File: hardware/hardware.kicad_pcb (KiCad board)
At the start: 2 copper layers, 83 x 54.5 mm, 15 parts, among them J1 Screw_Terminal_01x02, J2 Screw_Terminal_01x02, J3 Screw_Terminal_01x02, K1 RM85-2011-35-1005, K2 RM85-2011-35-1005, Q1 BC337, Q2 BC337, U1 XIAO-ESP32-C6

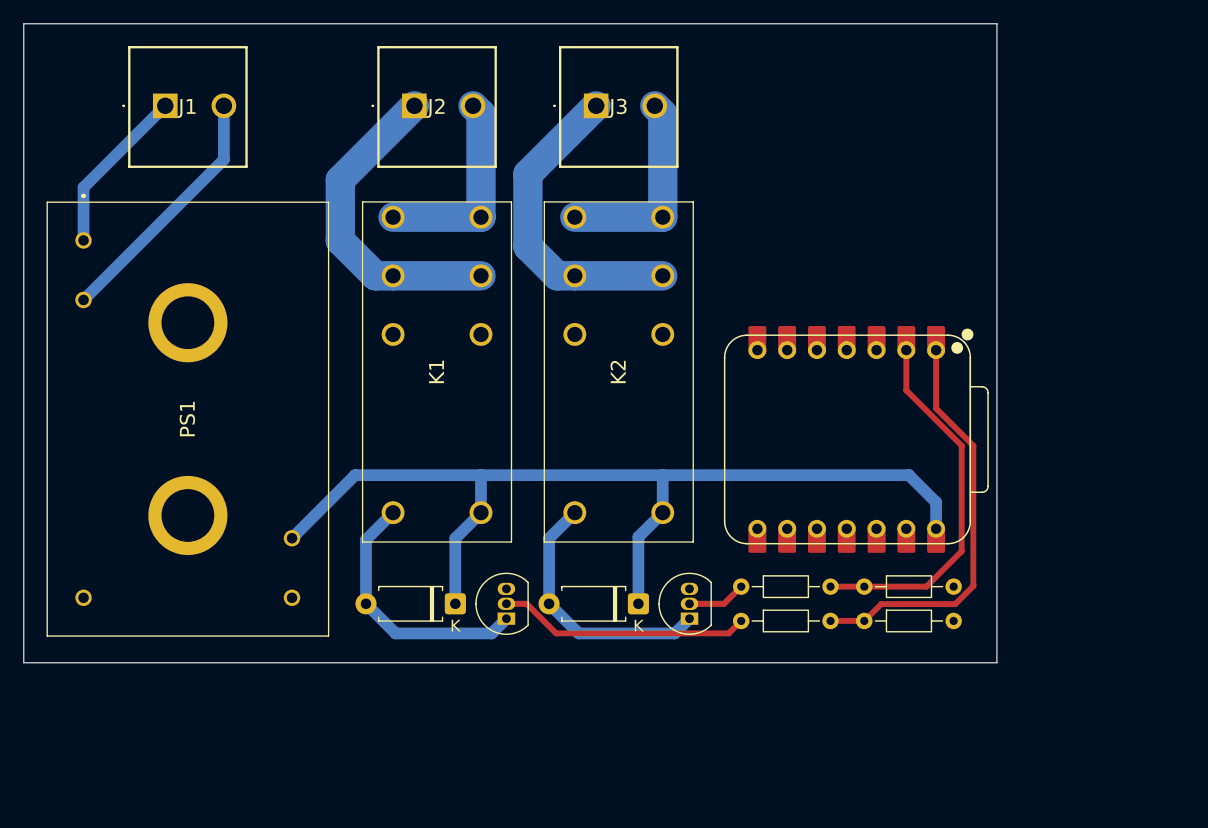
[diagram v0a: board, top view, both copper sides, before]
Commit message: Added GND fill zone
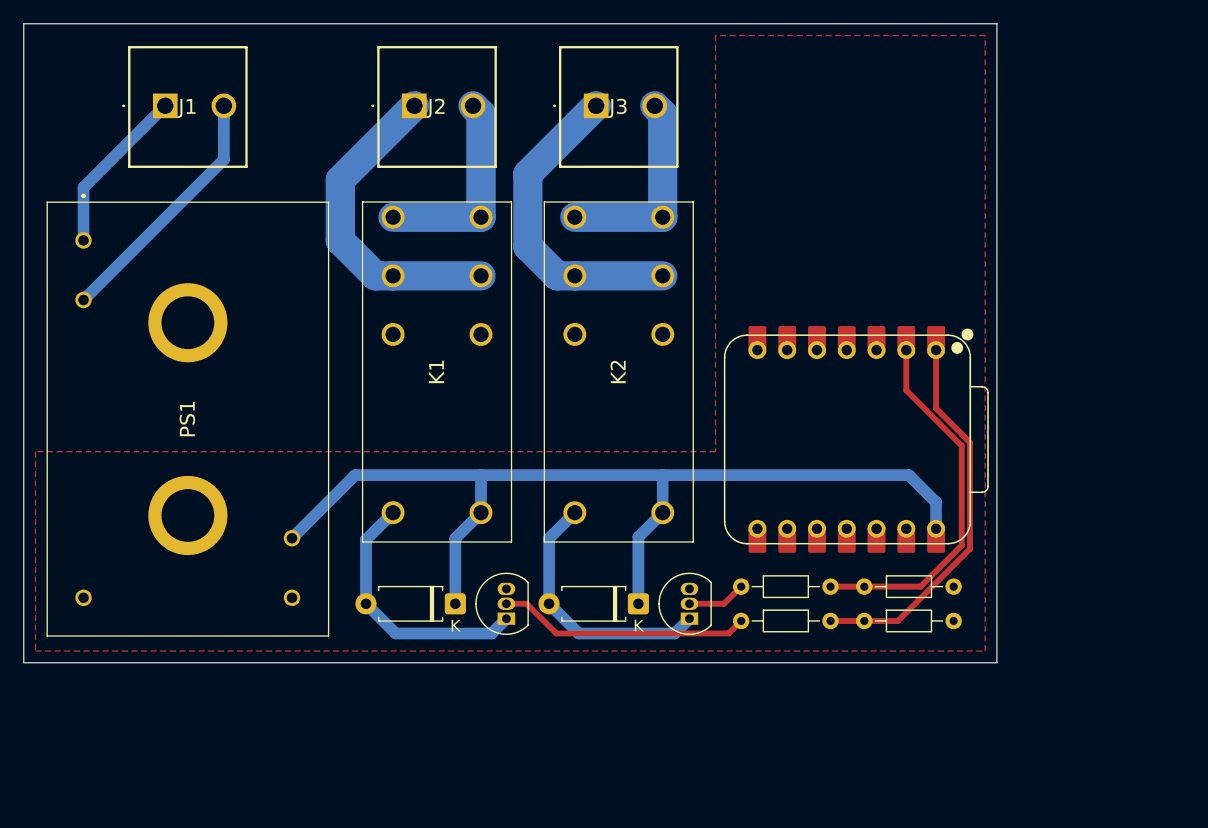
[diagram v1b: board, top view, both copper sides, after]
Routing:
- net RELAY_A_CTRL: track 34.9 -> 32.6 mm
- added copper zone on F.Cu, net GND
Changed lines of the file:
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@@
 	)
 	(segment
-		(start 88.12625 64.5)
-		(end 86.69 65.93625)
+		(start 92.8125 47.8125)
+		(end 92.8125 42.835)
 		(width 0.5)
 		(layer "F.Cu")
@@
 	)
 	(segment
-		(start 96 62.94651)
-		(end 94.44651 64.5)
+		(start 95 50.008636)
+		(end 95 50)
 		(width 0.5)
 		(layer "F.Cu")
@@
 	)
 	(segment
-		(start 94.44651 64.5)
-		(end 88.12625 64.5)
+		(start 89.555114 65.93625)
+		(end 95.701 59.790364)
 		(width 0.5)
 		(layer "F.Cu")
@@
 	)
 	(segment
-		(start 92.8125 42.835)
-		(end 92.8125 47.8125)
+		(start 95.701 50.709636)
+		(end 95 50.008636)
 		(width 0.5)
 		(layer "F.Cu")
@@
 	)
 	(segment
-		(start 92.8125 47.8125)
-		(end 96 51)
+		(start 86.69 65.93625)
+		(end 89.555114 65.93625)
 		(width 0.5)
 		(layer "F.Cu")
@@
 	)
 	(segment
-		(start 96 51)
-		(end 96 62.94651)
+		(start 95.701 59.790364)
+		(end 95.701 50.709636)
+		(width 0.5)
+		(layer "F.Cu")
+		(net 19)
+	)
+	(segment
+		(start 95 50)
+		(end 92.8125 47.8125)
 		(width 0.5)
 		(layer "F.Cu")
@@
 	)
 	(segment
-		(start 95 51)
-		(end 95 60)
-		(width 0.5)
-		(layer "F.Cu")
-		(net 20)
-	)
-	(segment
-		(start 91.99125 63.00875)
+		(start 83.81 63.00875)
 		(end 86.69 63.00875)
 		(width 0.5)
@@
 	)
 	(segment
-		(start 83.81 63.00875)
-		(end 86.69 63.00875)
+		(start 91.49125 63.00875)
+		(end 95 59.5)
+		(width 0.5)
+		(layer "F.Cu")
+		(net 20)
+	)
+	(segment
+		(start 86.69 63.00875)
+		(end 91.49125 63.00875)
 		(width 0.5)
 		(layer "F.Cu")
@@
 	)
 	(segment
-		(start 95 60)
-		(end 91.99125 63.00875)
+		(start 95 59.5)
+		(end 95 51)
 		(width 0.5)
 		(layer "F.Cu")
 		(net 20)
 	)
+	(zone
+		(net 16)
+		(net_name "GND")
+		(layer "F.Cu")
+		(hatch edge 0.5)
+		(connect_pads
+			(clearance 0.5)
+		)
+		(min_thickness 0.25)
+		(filled_areas_thickness no)
+		(fill yes
+			(thermal_gap 0.5)
+			(thermal_bridge_width 0.5)
+		)
+		(polygon
+			(pts
+				(xy 97 16) (xy 74 16) (xy 74 51.5) (xy 16 51.5) (xy 16 68.5) (xy 97 68.5)
+			)
+		)
+	)
 	(group ""

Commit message: Added mounting holes
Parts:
- added H1: MountingHole_Pad, MountingHole:MountingHole_2.2mm_M2_Pad, F.Cu at (110.0, 31.0)
- added H2: MountingHole, MountingHole:MountingHole_2.2mm_M2, F.Cu at (35.0, 31.0)
- moved D1 20.0 mm to (67.8, 76.5)
- moved D2 20.0 mm to (83.4, 76.5)
- moved K1 20.0 mm to (70.0, 48.5)
- moved K2 20.0 mm to (85.5, 48.5)
- moved R2 20.0 mm to (102.7, 78.0)
- moved R4 20.0 mm to (92.2, 78.0)
- moved U1 20.0 mm to (101.2, 62.5)
- moved J1 20.0 mm to (43.1, 34.0)
- moved J2 20.0 mm to (64.3, 34.0)
- moved J3 20.0 mm to (79.8, 34.0)
- moved PS1 20.0 mm to (36.1, 45.5)
- moved R5 20.0 mm to (92.2, 75.1)
- moved R6 20.0 mm to (102.7, 75.1)
- moved Q2 20.0 mm to (87.8, 77.8)
- moved Q1 20.0 mm to (72.2, 77.8)

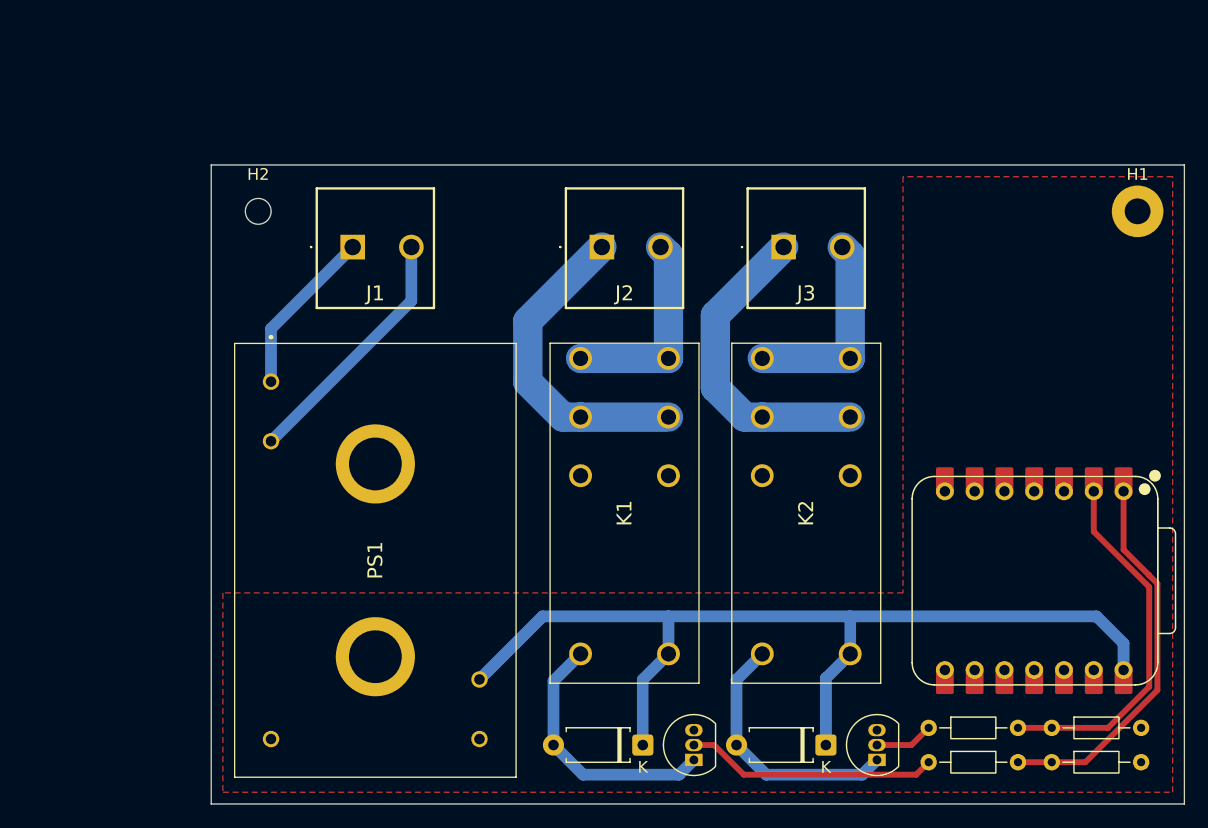
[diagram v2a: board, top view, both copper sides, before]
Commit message: Updated screw terminals
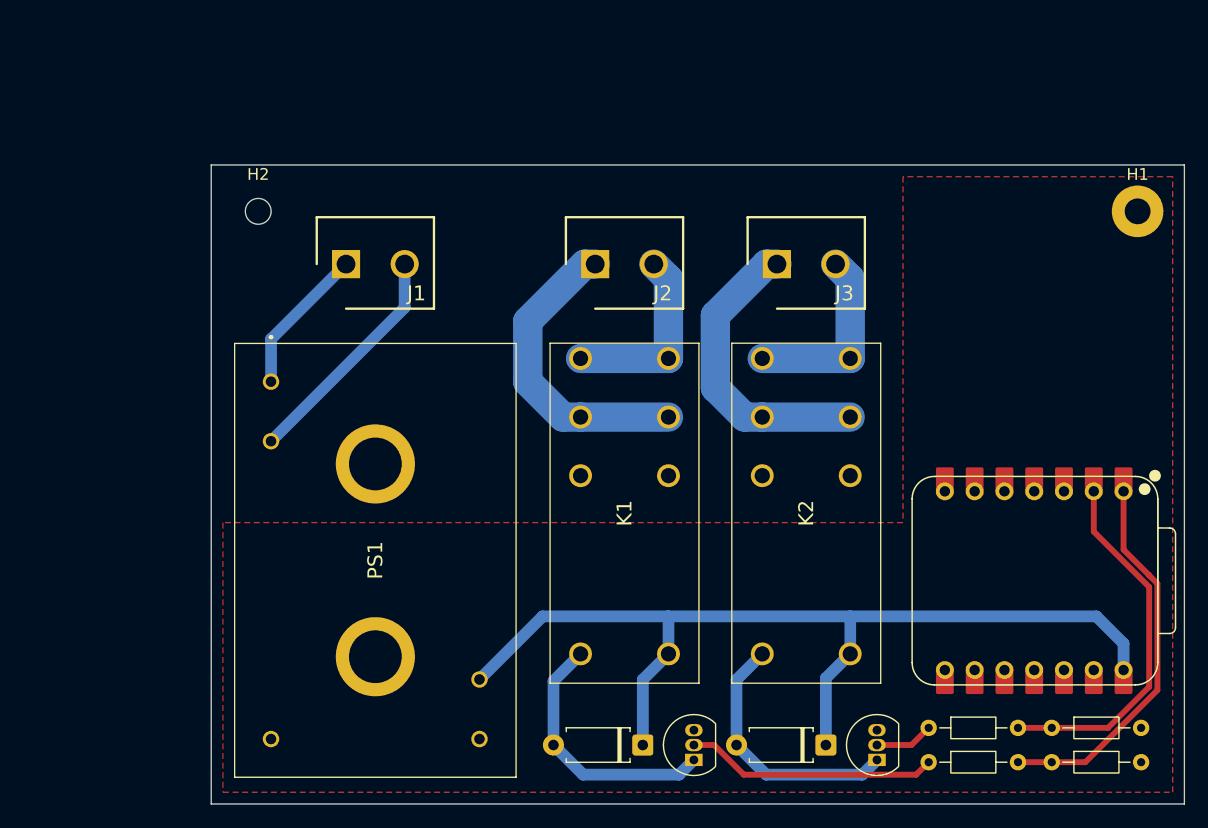
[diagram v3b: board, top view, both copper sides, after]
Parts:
- J1, J2, J3: footprint Degson Electronics:DG1285002P14 -> Degson Electronics:SHDR2W100P0X500_1X2_1000X780X1020P
- moved J1 1.56 mm to (42.5, 35.5)
- moved J2 1.56 mm to (63.7, 35.5)
- moved J3 1.56 mm to (79.2, 35.5)
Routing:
- net 230VAC_L: track 14.4 -> 12.7 mm
- net 230VAC_N: track 21.5 -> 19.8 mm
- net RELAY_B_OUT: track 17.3 -> 16.1 mm
- net RELAY_A_OUT: track 17.3 -> 16.1 mm
- net RELAY_A_IN: track 27.4 -> 26.2 mm
- net RELAY_B_IN: track 26.9 -> 25.8 mm

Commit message: Finished PCB layout and traces
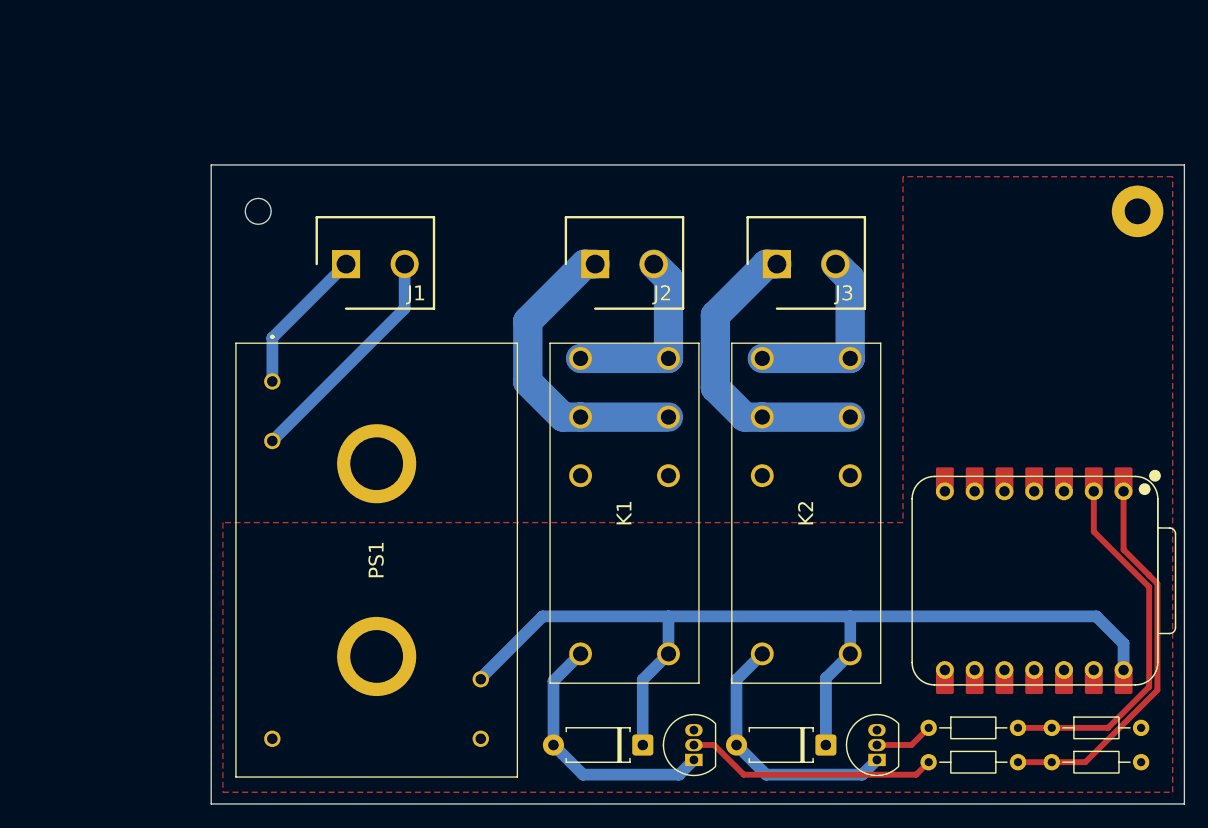
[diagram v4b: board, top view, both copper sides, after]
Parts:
- moved PS1 0.11 mm to (36.2, 45.5)
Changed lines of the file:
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@@
 	(net 29 "unconnected-(U1-GPIO19{slash}D8{slash}SCK-Pad9)")
 	(footprint "Degson Electronics:SHDR2W100P0X500_1X2_1000X780X1020P"
-		(locked yes)
 		(layer "F.Cu")
 		(at 79.239 35.5)
@@
 	)
 	(footprint "Degson Electronics:SHDR2W100P0X500_1X2_1000X780X1020P"
-		(locked yes)
 		(layer "F.Cu")
 		(at 63.739 35.5)
@@
 	)
 	(footprint "Diode_THT:D_A-405_P7.62mm_Horizontal"
-		(locked yes)
 		(layer "F.Cu")
 		(at 67.799 76.5175 180)
@@
 	(footprint "Mean Well:IRM0312"
 		(layer "F.Cu")
-		(at 36.089 45.525 -90)
+		(at 36.2 45.505 -90)
 		(descr "IRM-03-12-2")
 		(tags "Power Supply")
 		(property "Reference" "PS1"
-			(at 15.24 -8.9 270)
+			(at 15.24 -8.9 90)
 			(layer "F.SilkS")
 			(effects
@@
 		)
 		(property "Value" "IRM-03-5"
-			(at 15.24 -8.9 270)
+			(at 15.24 -8.9 90)
 			(layer "F.SilkS")
 			(hide yes)
@@
 		)
 		(property "Datasheet" "https://www.meanwell.com/Upload/PDF/IRM-03/IRM-03-SPEC.PDF"
-			(at 0 0 270)
+			(at 0 0 90)
 			(layer "F.Fab")
 			(hide yes)
@@
 		)
 		(property "Description" "Mean Well 3W Encapsulated Switch Mode Power Supply, 0  600mA, 5V dc"
-			(at 0 0 270)
+			(at 0 0 90)
 			(layer "F.Fab")
 			(hide yes)
@@
 		)
 		(fp_text user "${REFERENCE}"
-			(at 15.24 -8.9 270)
+			(at 15.24 -8.9 90)
 			(layer "F.Fab")
 			(effects
@@
 	)
 	(footprint "Diode_THT:D_A-405_P7.62mm_Horizontal"
-		(locked yes)
 		(layer "F.Cu")
 		(at 83.412333 76.5175 180)
@@
 	)
 	(footprint "Package_TO_SOT_THT:TO-92_Inline"
-		(locked yes)
 		(layer "F.Cu")
 		(at 87.769 77.7875 90)
@@
 	)
 	(footprint "Degson Electronics:SHDR2W100P0X500_1X2_1000X780X1020P"
-		(locked yes)
 		(layer "F.Cu")
 		(at 42.489 35.5)
@@
 	)
 	(footprint "Resistor_THT:R_Axial_DIN0204_L3.6mm_D1.6mm_P7.62mm_Horizontal"
-		(locked yes)
 		(layer "F.Cu")
 		(at 92.179 75.05375)
@@
 	)
 	(footprint "Resistor_THT:R_Axial_DIN0204_L3.6mm_D1.6mm_P7.62mm_Horizontal"
-		(locked yes)
 		(layer "F.Cu")
 		(at 92.179 77.98125)
@@
 			(at 0 -3.15 0)
 			(layer "F.SilkS")
+			(hide yes)
 			(effects
 				(font
@@
 			(at 0 3.15 0)
 			(layer "F.Fab")
+			(hide yes)
 			(effects
 				(font
@@
 	)
 	(footprint "Relpol:relpol_rm85_2011_35_1005"
-		(locked yes)
 		(layer "F.Cu")
 		(at 85.489 48.545 90)
@@
 	)
 	(footprint "Resistor_THT:R_Axial_DIN0204_L3.6mm_D1.6mm_P7.62mm_Horizontal"
-		(locked yes)
 		(layer "F.Cu")
 		(at 102.679 75.05375)
@@
 	)
 	(footprint "Resistor_THT:R_Axial_DIN0204_L3.6mm_D1.6mm_P7.62mm_Horizontal"
-		(locked yes)
 		(layer "F.Cu")
 		(at 102.679 77.98125)
@@
 	)
 	(footprint "Relpol:relpol_rm85_2011_35_1005"
-		(locked yes)
 		(layer "F.Cu")
 		(at 69.989 48.545 90)
@@
 	)
 	(footprint "Package_TO_SOT_THT:TO-92_Inline"
-		(locked yes)
 		(layer "F.Cu")
 		(at 72.155667 77.7875 90)
@@
 			(at 0 -3.15 0)
 			(layer "F.SilkS")
+			(hide yes)
 			(effects
 				(font
@@
 			(at 0 3.15 0)
 			(layer "F.Fab")
+			(hide yes)
 			(effects
 				(font
@@
 	)
 	(segment
-		(start 47.489 39.205)
-		(end 36.089 50.605)
+		(start 36.2 50.585)
+		(end 47.489 39.296)
 		(width 1)
 		(layer "B.Cu")
@@
 	)
 	(segment
-		(start 47.489 35.5)
-		(end 47.489 39.205)
+		(start 47.489 39.296)
+		(end 47.489 35.5)
 		(width 1)
 		(layer "B.Cu")
@@
 	)
 	(segment
-		(start 36.089 41.9)
-		(end 42.489 35.5)
+		(start 36.2 45.505)
+		(end 36.2 41.789)
 		(width 1)
 		(layer "B.Cu")
@@
 	)
 	(segment
-		(start 36.089 45.525)
-		(end 36.089 41.9)
+		(start 36.2 41.789)
+		(end 42.489 35.5)
 		(width 1)
 		(layer "B.Cu")
@@
 		)
 	)
-	(group ""
-		(locked yes)
-		(members "14a449ef-729f-4ec5-97c7-8f9b6c2a9ec5" "a298fca7-4b70-459b-91ac-bc5e14cbd615")
-	)
-	(group ""
-		(locked yes)
-		(members "193541c9-0b7f-4fc5-80d9-b2d7a9f955e9" "ebdf6087-87fd-4a03-8f10-9fd73c53aa03")
-	)
-	(group ""
-		(locked yes)
-		(members "877d0a72-a6c9-4e6c-8d44-23fb2af5e1b2" "e3708ea3-edfd-490d-9bbd-8f41a998a06c")
-	)
-	(group ""
-		(locked yes)
-		(members "a0e70d2d-c3c3-4f06-abc8-31bdfc192c5a" "bb0645df-9655-4da6-ac53-f84146cd414f")
-	)
-	(group ""
-		(locked yes)
-		(members "32c08bd7-5708-4592-8438-7871637da772" "7baacf06-e9cf-4839-bfe1-9916ae24fdbd"
-			"7bd5ea53-670a-4ff2-a470-c5db6ed7a409" "f2411101-6095-4539-bf13-fa4f6e961653"
-		)
-	)
-	(group ""
-		(locked yes)
-		(members "91095277-18f8-43cb-9cb7-3ecdf36fb600" "a8b52843-777d-4577-8115-ab1fa7c34520")
-	)
 	(embedded_fonts no)

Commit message: Finished PCB silkscreen
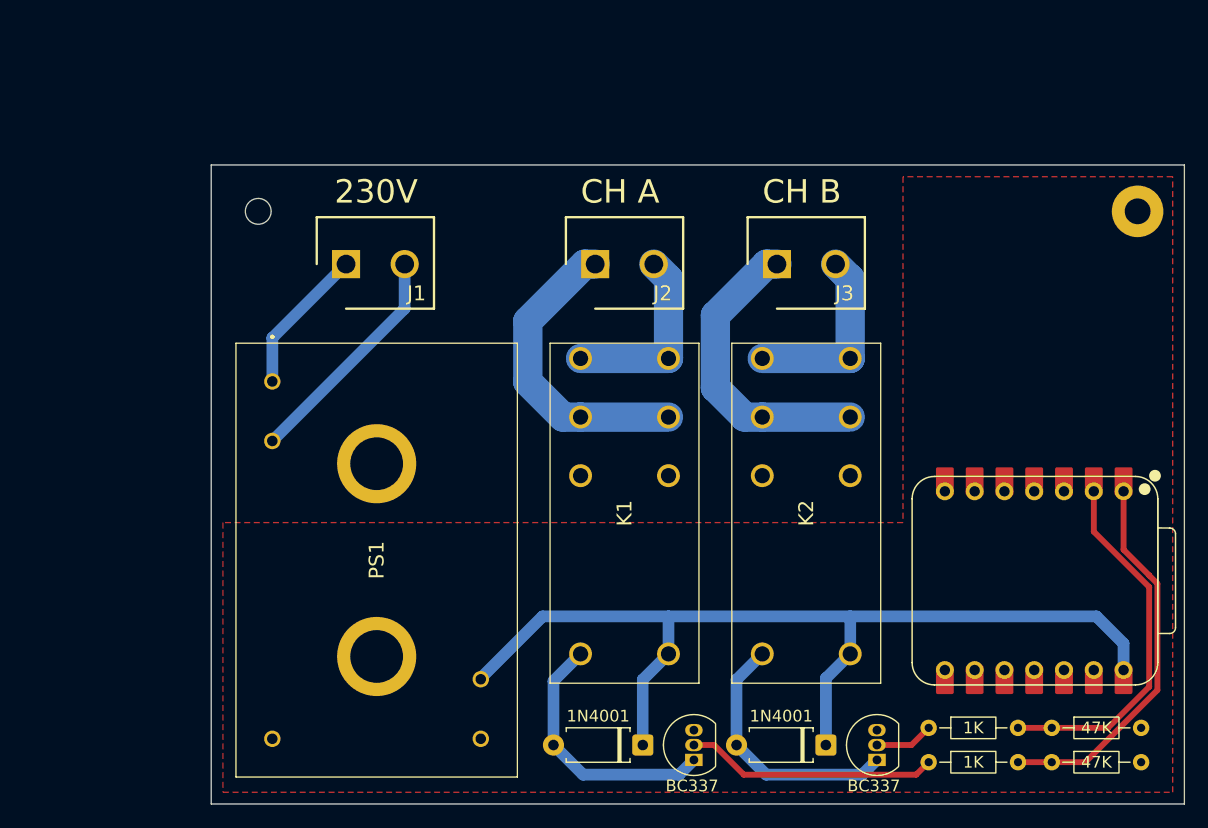
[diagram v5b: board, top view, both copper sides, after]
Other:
- board text added: "230V"
- board text added: "CH A"
- board text added: "CH B"
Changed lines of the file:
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@@
 		(property "Value" "1N4001"
 			(at 3.81 2.47 0)
-			(layer "F.Fab")
-			(hide yes)
+			(layer "F.SilkS")
 			(effects
 				(font
@@
 		(property "Value" "1N4001"
 			(at 3.81 2.47 0)
-			(layer "F.Fab")
-			(hide yes)
+			(layer "F.SilkS")
 			(effects
 				(font
@@
 		)
 		(property "Value" "BC337"
-			(at 1.47 15.55 90)
-			(layer "F.Fab")
-			(hide yes)
+			(at -2.2125 -0.269 180)
+			(layer "F.SilkS")
 			(effects
 				(font
@@
 		)
 		(property "Value" "1K"
-			(at 2.71 5.22 0)
-			(layer "F.Fab")
-			(hide yes)
-			(effects
-				(font
-					(size 1 1)
-					(thickness 0.15)
+			(at 3.81 0 0)
+			(layer "F.SilkS")
+			(effects
+				(font
+					(size 1 1)
+					(thickness 0.125)
 				)
 			)
@@
 		)
 		(property "Value" "1K"
-			(at 3.81 1.92 0)
-			(layer "F.Fab")
-			(hide yes)
-			(effects
-				(font
-					(size 1 1)
-					(thickness 0.15)
+			(at 3.81 0 0)
+			(layer "F.SilkS")
+			(effects
+				(font
+					(size 1 1)
+					(thickness 0.125)
 				)
 			)
@@
 		)
 		(property "Value" "47K"
-			(at -30.48 23.03 0)
-			(layer "F.Fab")
-			(hide yes)
-			(effects
-				(font
-					(size 1 1)
-					(thickness 0.15)
+			(at 3.81 0 0)
+			(layer "F.SilkS")
+			(effects
+				(font
+					(size 1 1)
+					(thickness 0.125)
 				)
 			)
@@
 		)
 		(property "Value" "47K"
-			(at 3.81 1.92 0)
-			(layer "F.Fab")
-			(hide yes)
-			(effects
-				(font
-					(size 1 1)
-					(thickness 0.15)
+			(at 3.81 0 0)
+			(layer "F.SilkS")
+			(effects
+				(font
+					(size 1 1)
+					(thickness 0.125)
 				)
 			)
@@
 		)
 		(property "Value" "BC337"
-			(at 1.27 2.79 90)
-			(layer "F.Fab")
-			(hide yes)
+			(at -2.2125 -0.155667 180)
+			(layer "F.SilkS")
 			(effects
 				(font
@@
 		(layer "Edge.Cuts")
 	)
+	(gr_text "230V"
+		(at 41.5 30.5 0)
+		(layer "F.SilkS")
+		(effects
+			(font
+				(size 2 2)
+				(thickness 0.25)
+			)
+			(justify left bottom)
+		)
+	)
+	(gr_text "CH B"
+		(at 78 30.5 0)
+		(layer "F.SilkS")
+		(effects
+			(font
+				(size 2 2)
+				(thickness 0.25)
+			)
+			(justify left bottom)
+		)
+	)
+	(gr_text "CH A"
+		(at 62.5 30.5 0)
+		(layer "F.SilkS")
+		(effects
+			(font
+				(size 2 2)
+				(thickness 0.25)
+			)
+			(justify left bottom)
+		)
+	)
 	(segment
